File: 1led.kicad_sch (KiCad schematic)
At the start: 2 parts

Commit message: push button
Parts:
- added SW1: SW_Push, symbol Switch:SW_Push
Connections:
- net at D1.1 (K): now also SW1.2
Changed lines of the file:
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@@
+	(wire
+		(pts
+			(xy 114.3 72.39) (xy 127 72.39)
+		)
+		(stroke
+			(width 0)
+			(type default)
+		)
+	)
 	(wire
 		(pts
@@
 	(wire
 		(pts
-			(xy 124.46 72.39) (xy 127 72.39)
-		)
-		(stroke
-			(width 0)
-			(type default)
-		)
-	)
-	(wire
-		(pts
 			(xy 134.62 72.39) (xy 152.4 72.39)
+		)
+		(stroke
+			(width 0)
+			(type default)
+		)
+	)
+	(wire
+		(pts
+			(xy 100.33 72.39) (xy 104.14 72.39)
 		)
 		(stroke
@@
 					(unit 1)
 				)
+			)
+		)
+	)
+	(symbol
+		(lib_id "Switch:SW_Push")
+		(at 109.22 72.39 0)
+		(unit 1)
+		(exclude_from_sim no)
+		(in_bom yes)
+		(on_board yes)
+		(dnp no)
+		(fields_autoplaced yes)
+		(property "Reference" "SW1"
+			(at 109.22 64.77 0)
+			(effects
+				(font
+					(size 1.27 1.27)
+				)
+			)
+		)
+		(property "Value" "SW_Push"
+			(at 109.22 67.31 0)
+			(effects
+				(font
+					(size 1.27 1.27)
+				)
+			)
+		)
+		(property "Footprint" ""
+			(at 109.22 67.31 0)
+			(effects
+				(font
+					(size 1.27 1.27)
+				)
+				(hide yes)
+			)
+		)
+		(property "Datasheet" "~"
+			(at 109.22 67.31 0)
+			(effects
+				(font
+					(size 1.27 1.27)
+				)
+				(hide yes)
+			)
+		)
+		(property "Description" "Push button switch, generic, two pins"
+			(at 109.22 72.39 0)
+			(effects
+				(font
+					(size 1.27 1.27)
+				)
+				(hide yes)
+			)
+		)
+		(pin "2"
+		)
+		(pin "1"
+		)
+		(instances
+			(project ""
+				(path "/c023133a-7389-44bb-8cb6-85f9b54b2e54"
+					(reference "SW1")
+					(unit 1)
+				)

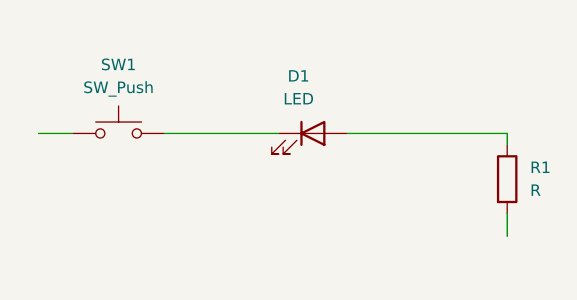
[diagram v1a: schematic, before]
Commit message: battery added
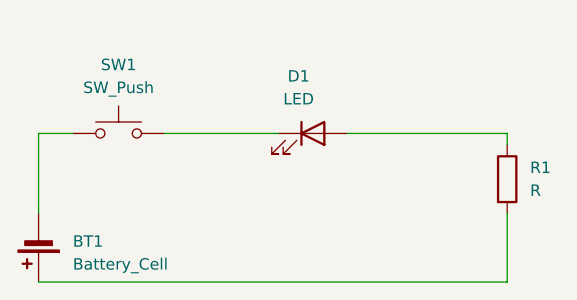
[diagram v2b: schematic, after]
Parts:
- added BT1: Battery_Cell, symbol Device:Battery_Cell
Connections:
- net at R1.2: now also BT1.1 (+)
- net at SW1.1: now also BT1.2 (-)
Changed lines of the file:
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@@
 	(wire
 		(pts
-			(xy 152.4 81.28) (xy 152.4 83.82)
+			(xy 100.33 88.9) (xy 152.4 88.9)
+		)
+		(stroke
+			(width 0)
+			(type default)
+		)
+	)
+	(wire
+		(pts
+			(xy 152.4 81.28) (xy 152.4 88.9)
+		)
+		(stroke
+			(width 0)
+			(type default)
+		)
+	)
+	(wire
+		(pts
+			(xy 100.33 72.39) (xy 100.33 81.28)
 		)
 		(stroke
@@
 					(unit 1)
 				)
+			)
+		)
+	)
+	(symbol
+		(lib_id "Device:Battery_Cell")
+		(at 100.33 83.82 180)
+		(unit 1)
+		(exclude_from_sim no)
+		(in_bom yes)
+		(on_board yes)
+		(dnp no)
+		(fields_autoplaced yes)
+		(property "Reference" "BT1"
+			(at 104.14 84.3914 0)
+			(effects
+				(font
+					(size 1.27 1.27)
+				)
+				(justify right)
+			)
+		)
+		(property "Value" "Battery_Cell"
+			(at 104.14 86.9314 0)
+			(effects
+				(font
+					(size 1.27 1.27)
+				)
+				(justify right)
+			)
+		)
+		(property "Footprint" ""
+			(at 100.33 85.344 90)
+			(effects
+				(font
+					(size 1.27 1.27)
+				)
+				(hide yes)
+			)
+		)
+		(property "Datasheet" "~"
+			(at 100.33 85.344 90)
+			(effects
+				(font
+					(size 1.27 1.27)
+				)
+				(hide yes)
+			)
+		)
+		(property "Description" "Single-cell battery"
+			(at 100.33 83.82 0)
+			(effects
+				(font
+					(size 1.27 1.27)
+				)
+				(hide yes)
+			)
+		)
+		(pin "1"
+		)
+		(pin "2"
+		)
+		(instances
+			(project ""
+				(path "/c023133a-7389-44bb-8cb6-85f9b54b2e54"
+					(reference "BT1")
+					(unit 1)
+				)

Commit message: 2led added
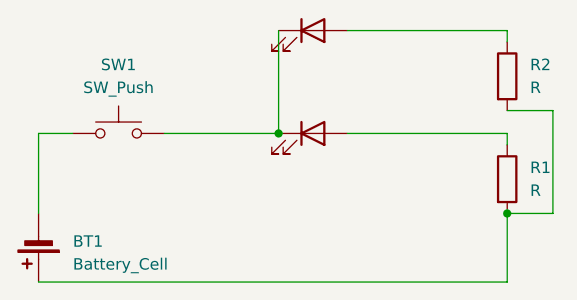
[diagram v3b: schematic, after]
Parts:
- added D2: LED, symbol Device:LED
- added R2: R, symbol Device:R
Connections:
- net at BT1.1 (+), R1.2: now also R2.2
- net at D1.1 (K), SW1.2: now also D2.1 (K)
- new net: D2.2 (A), R2.1
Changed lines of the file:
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@@
 	(generator_version "8.0")
 	(paper "A4")
+	(junction
+		(at 152.4 81.28)
+		(diameter 0)
+		(color 0 0 0 0)
+	)
+	(junction
+		(at 127 72.39)
+		(diameter 0)
+		(color 0 0 0 0)
+	)
 	(wire
 		(pts
@@
 	(wire
 		(pts
+			(xy 157.48 69.85) (xy 152.4 69.85)
+		)
+		(stroke
+			(width 0)
+			(type default)
+		)
+	)
+	(wire
+		(pts
+			(xy 127 60.96) (xy 127 72.39)
+		)
+		(stroke
+			(width 0)
+			(type default)
+		)
+	)
+	(wire
+		(pts
 			(xy 152.4 81.28) (xy 152.4 88.9)
 		)
@@
 	(wire
 		(pts
+			(xy 134.62 60.96) (xy 152.4 60.96)
+		)
+		(stroke
+			(width 0)
+			(type default)
+		)
+	)
+	(wire
+		(pts
 			(xy 100.33 72.39) (xy 100.33 81.28)
 		)
@@
 	(wire
 		(pts
+			(xy 152.4 81.28) (xy 157.48 81.28)
+		)
+		(stroke
+			(width 0)
+			(type default)
+		)
+	)
+	(wire
+		(pts
 			(xy 134.62 72.39) (xy 152.4 72.39)
+		)
+		(stroke
+			(width 0)
+			(type default)
+		)
+	)
+	(wire
+		(pts
+			(xy 152.4 60.96) (xy 152.4 62.23)
+		)
+		(stroke
+			(width 0)
+			(type default)
+		)
+	)
+	(wire
+		(pts
+			(xy 157.48 81.28) (xy 157.48 69.85)
 		)
 		(stroke
@@
 	)
 	(symbol
+		(lib_id "Device:LED")
+		(at 130.81 60.96 0)
+		(unit 1)
+		(exclude_from_sim no)
+		(in_bom yes)
+		(on_board yes)
+		(dnp no)
+		(fields_autoplaced yes)
+		(property "Reference" "D2"
+			(at 129.2225 54.61 0)
+			(effects
+				(font
+					(size 1.27 1.27)
+				)
+				(hide yes)
+			)
+		)
+		(property "Value" "LED"
+			(at 129.2225 57.15 0)
+			(effects
+				(font
+					(size 1.27 1.27)
+				)
+				(hide yes)
+			)
+		)
+		(property "Footprint" ""
+			(at 130.81 60.96 0)
+			(effects
+				(font
+					(size 1.27 1.27)
+				)
+				(hide yes)
+			)
+		)
+		(property "Datasheet" "~"
+			(at 130.81 60.96 0)
+			(effects
+				(font
+					(size 1.27 1.27)
+				)
+				(hide yes)
+			)
+		)
+		(property "Description" "Light emitting diode"
+			(at 130.81 60.96 0)
+			(effects
+				(font
+					(size 1.27 1.27)
+				)
+				(hide yes)
+			)
+		)
+		(pin "1"
+		)
+		(pin "2"
+		)
+		(instances
+			(project "1led"
+				(path "/c023133a-7389-44bb-8cb6-85f9b54b2e54"
+					(reference "D2")
+					(unit 1)
+				)
+			)
+		)
+	)
+	(symbol
 		(lib_id "Device:Battery_Cell")
 		(at 100.33 83.82 180)
@@
 				(path "/c023133a-7389-44bb-8cb6-85f9b54b2e54"
 					(reference "BT1")
+					(unit 1)
+				)
+			)
+		)
+	)
+	(symbol
+		(lib_id "Device:R")
+		(at 152.4 66.04 0)
+		(unit 1)
+		(exclude_from_sim no)
+		(in_bom yes)
+		(on_board yes)
+		(dnp no)
+		(fields_autoplaced yes)
+		(property "Reference" "R2"
+			(at 154.94 64.7699 0)
+			(effects
+				(font
+					(size 1.27 1.27)
+				)
+				(justify left)
+			)
+		)
+		(property "Value" "R"
+			(at 154.94 67.3099 0)
+			(effects
+				(font
+					(size 1.27 1.27)
+				)
+				(justify left)
+			)
+		)
+		(property "Footprint" ""
+			(at 150.622 66.04 90)
+			(effects
+				(font
+					(size 1.27 1.27)
+				)
+				(hide yes)
+			)
+		)
+		(property "Datasheet" "~"
+			(at 152.4 66.04 0)
+			(effects
+				(font
+					(size 1.27 1.27)
+				)
+				(hide yes)
+			)
+		)
+		(property "Description" "Resistor"
+			(at 152.4 66.04 0)
+			(effects
+				(font
+					(size 1.27 1.27)
+				)
+				(hide yes)
+			)
+		)
+		(pin "1"
+		)
+		(pin "2"
+		)
+		(instances
+			(project "1led"
+				(path "/c023133a-7389-44bb-8cb6-85f9b54b2e54"
+					(reference "R2")
 					(unit 1)
 				)
@@
 					(size 1.27 1.27)
 				)
+				(hide yes)
 			)
 		)
@@
 					(size 1.27 1.27)
 				)
-			)
-		)
+				(hide yes)
+			)
+		)
